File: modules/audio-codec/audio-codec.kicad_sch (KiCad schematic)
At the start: 1 part, among them U1 TLV320AIC3110IRHBR

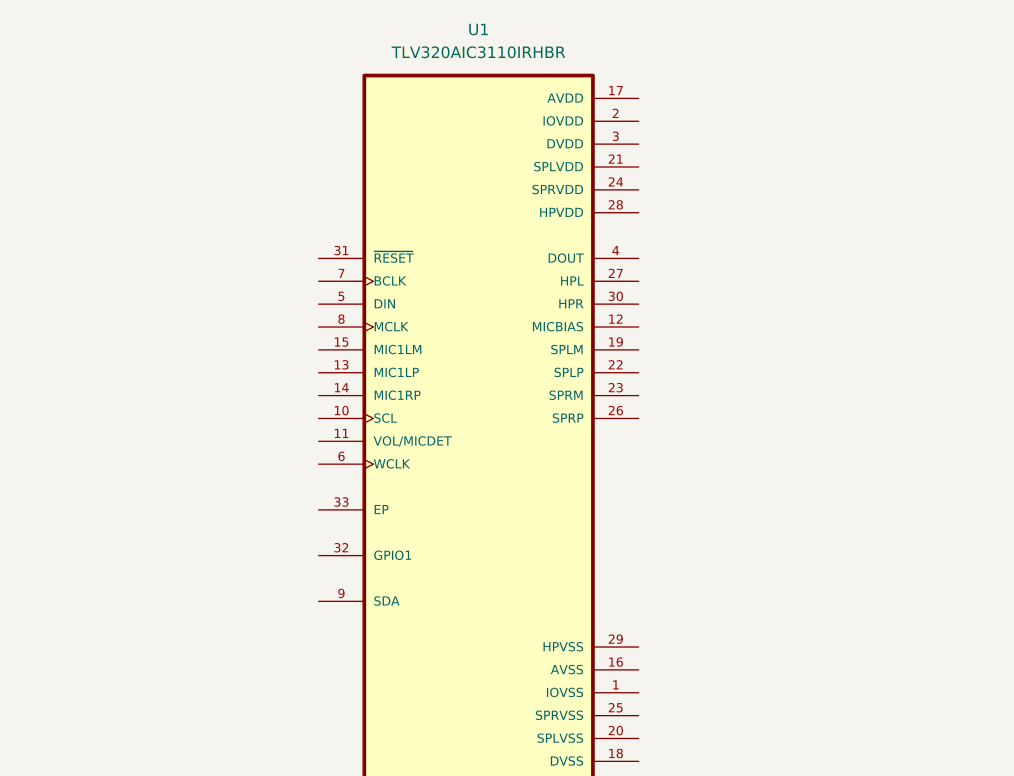
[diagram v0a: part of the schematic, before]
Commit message: add ADP5301 vreg and work on schematic
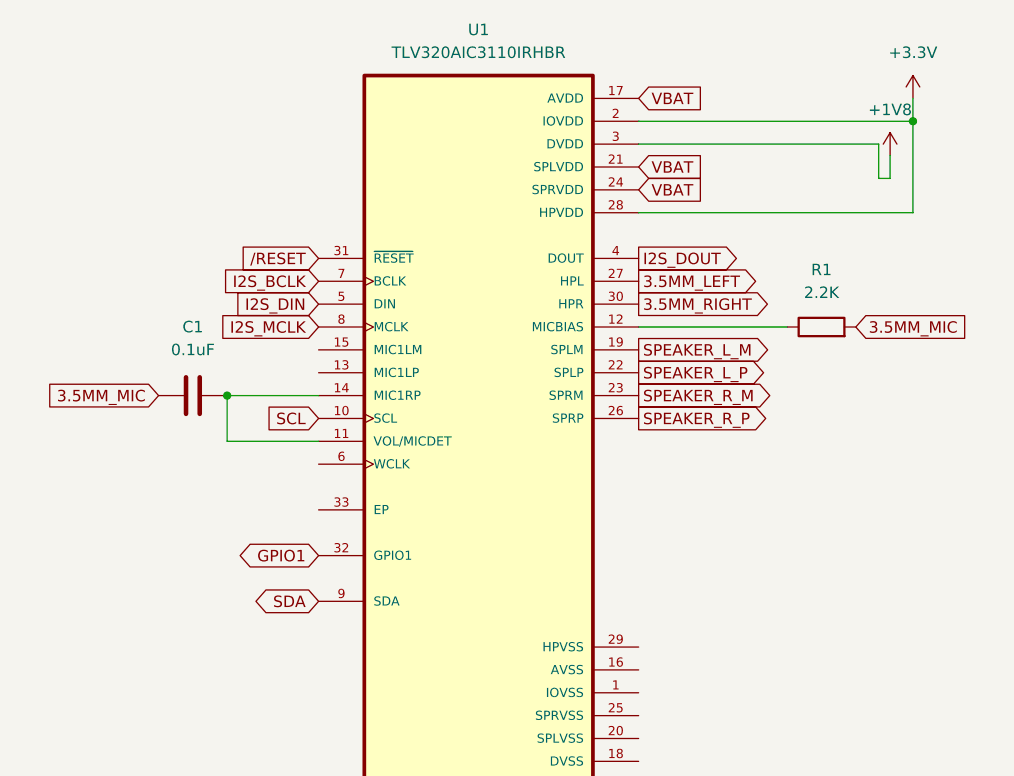
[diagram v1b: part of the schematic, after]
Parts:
- added C1: 0.1uF, symbol Device:C
- added R1: 2.2K, symbol Device:R
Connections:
- net SCL: now reaches U1.10 (SCL)
- net at U1.11 (VOL/MICDET): now also U1.14 (MIC1RP), C1.1
- net at U1.12 (MICBIAS): now also R1.1
- net VBAT: now reaches U1.17 (AVDD)
- net VBAT: now also U1.21 (SPLVDD), U1.24 (SPRVDD)
- net SPEAKER_L_M: now reaches U1.19 (SPLM)
- net +3.3V: now reaches U1.2 (IOVDD)
- net +3.3V: now also U1.28 (HPVDD)
- net SPEAKER_L_P: now reaches U1.22 (SPLP)
- net SPEAKER_R_M: now reaches U1.23 (SPRM)
- net SPEAKER_R_P: now reaches U1.26 (SPRP)
- net 3.5MM_LEFT: now reaches U1.27 (HPL)
- net +1V8: now reaches U1.3 (DVDD)
- net 3.5MM_RIGHT: now reaches U1.30 (HPR)
- net /RESET: now reaches U1.31 (~{RESET})
- net GPIO1: now reaches U1.32 (GPIO1)
- net I2S_DOUT: now reaches U1.4 (DOUT)
- net I2S_DIN: now reaches U1.5 (DIN)
- net I2S_BCLK: now reaches U1.7 (BCLK)
- net I2S_MCLK: now reaches U1.8 (MCLK)
- net SDA: now reaches U1.9 (SDA)
- new net 3.5MM_MIC: C1.2, R1.2

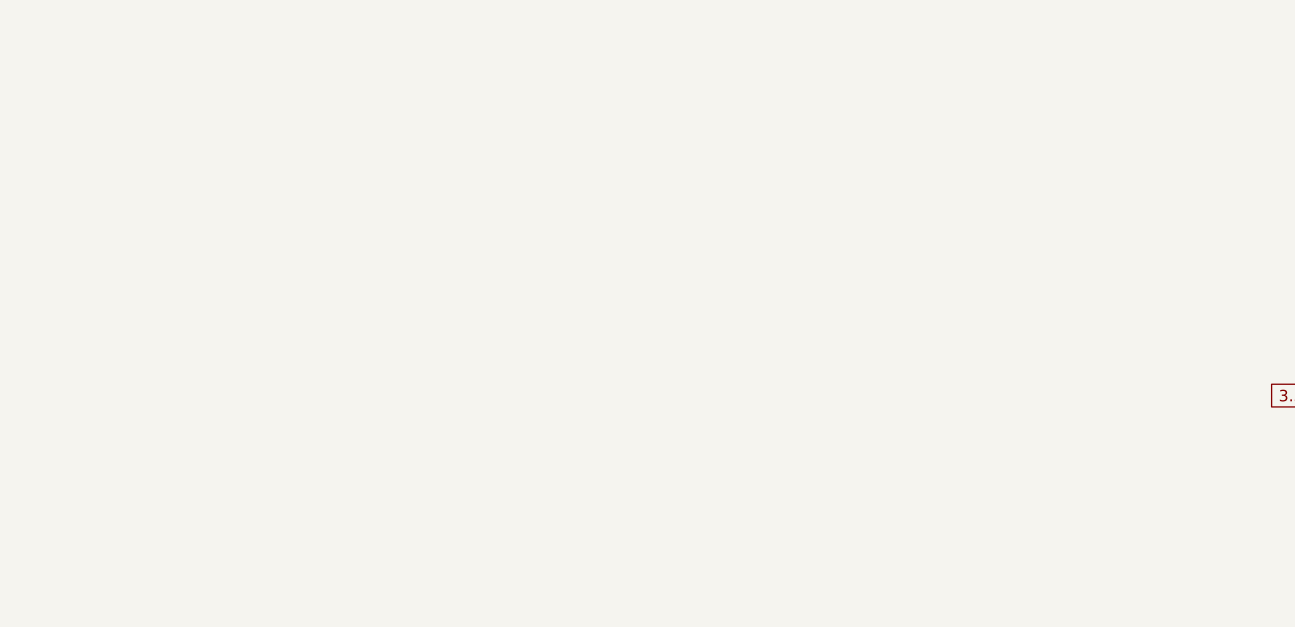
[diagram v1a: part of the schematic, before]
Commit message: more work on audio codec module
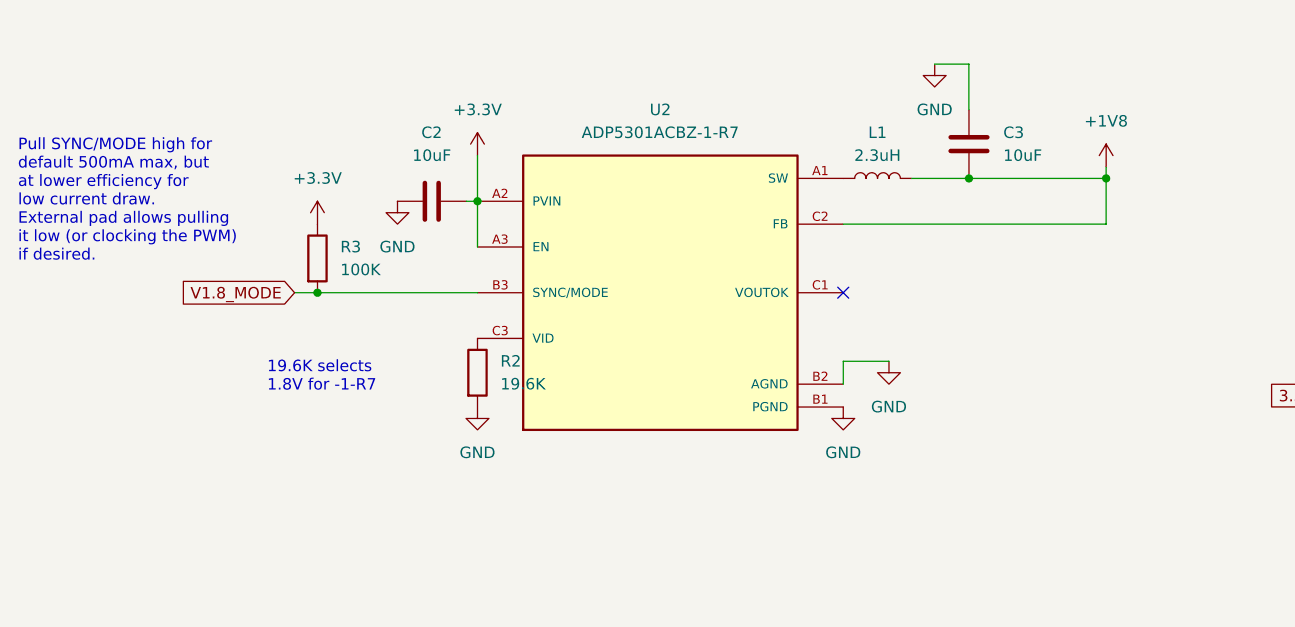
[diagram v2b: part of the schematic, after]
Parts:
- added C2, C3: 10uF, symbol Device:C
- added L1: 2.3uH, symbol Device:L
- added R2: 19.6K, symbol Device:R
- added R3: 100K, symbol Device:R
- added U2: ADP5301ACBZ-1-R7, ADP5301ACBZ-1-R7:BGA9C50P3X3_187X165X66N, symbol ADP5301ACBZ-1-R7:ADP5301ACBZ-1-R7
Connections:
- net +1V8: now also C3.1, L1.2, U2.C2 (FB)
- net +3.3V: now also C2.2, R3.1, U2.A2 (PVIN), U2.A3 (EN)
- new net: L1.1, U2.A1 (SW)
- new net: R2.1, U2.C3 (VID)
- new net GND: C2.1, C3.2, R2.2, U2.B1 (PGND), U2.B2 (AGND)
- new net V1.8_MODE: R3.2, U2.B3 (SYNC/MODE)
- no-connect marks 0 -> 1
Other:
- note added: "19.6K selects 1.8V for -1-R7"
- note added: "Pull SYNC/MODE high for default 500mA max, but at lower efficiency for low current draw. External pad allows pulling it low (or clocking the PWM) if desired."

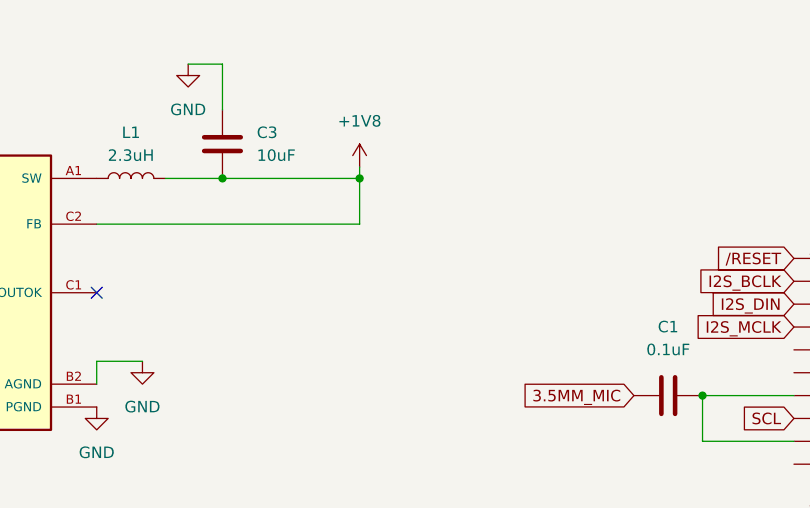
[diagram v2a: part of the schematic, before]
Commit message: add 1.8V test point
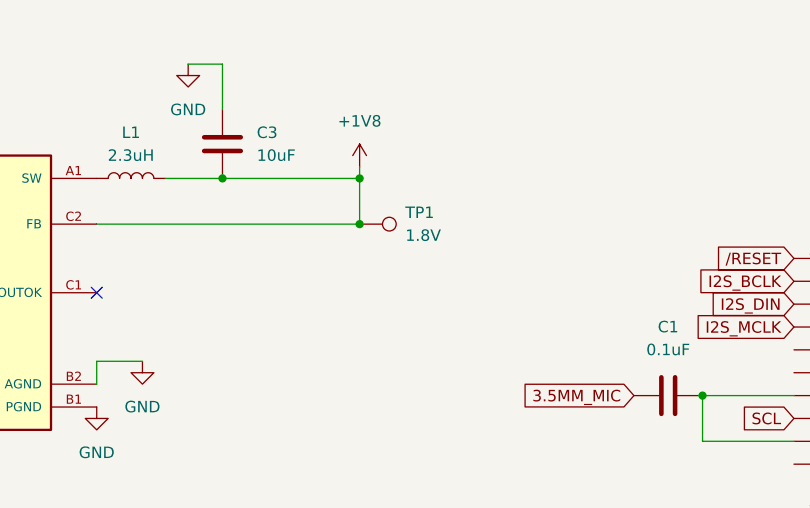
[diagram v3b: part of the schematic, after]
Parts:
- added TP1: 1.8V, symbol Connector:TestPoint
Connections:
- net +1V8: now also TP1.1
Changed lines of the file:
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@@
+	)
+	(junction
+		(at 134.62 57.15)
+		(diameter 0)
+		(color 0 0 0 0)
 	)
 	(junction
@@
 					(unit 1)
 				)
+			)
+		)
+	)
+	(symbol
+		(lib_id "Connector:TestPoint")
+		(at 134.62 57.15 270)
+		(unit 1)
+		(exclude_from_sim no)
+		(in_bom yes)
+		(on_board yes)
+		(dnp no)
+		(fields_autoplaced yes)
+		(property "Reference" "TP1"
+			(at 139.7 55.8799 90)
+			(effects
+				(font
+					(size 1.27 1.27)
+				)
+				(justify left)
+			)
+		)
+		(property "Value" "1.8V"
+			(at 139.7 58.4199 90)
+			(effects
+				(font
+					(size 1.27 1.27)
+				)
+				(justify left)
+			)
+		)
+		(property "Footprint" ""
+			(at 134.62 62.23 0)
+			(effects
+				(font
+					(size 1.27 1.27)
+				)
+				(hide yes)
+			)
+		)
+		(property "Datasheet" "~"
+			(at 134.62 62.23 0)
+			(effects
+				(font
+					(size 1.27 1.27)
+				)
+				(hide yes)
+			)
+		)
+		(property "Description" "test point"
+			(at 134.62 57.15 0)
+			(effects
+				(font
+					(size 1.27 1.27)
+				)
+				(hide yes)
+			)
+		)
+		(pin "1"
+		)
+		(instances
+			(project ""
+				(path "/e0031877-65b0-4e57-86fe-bc20869de862"
+					(reference "TP1")
+					(unit 1)
+				)

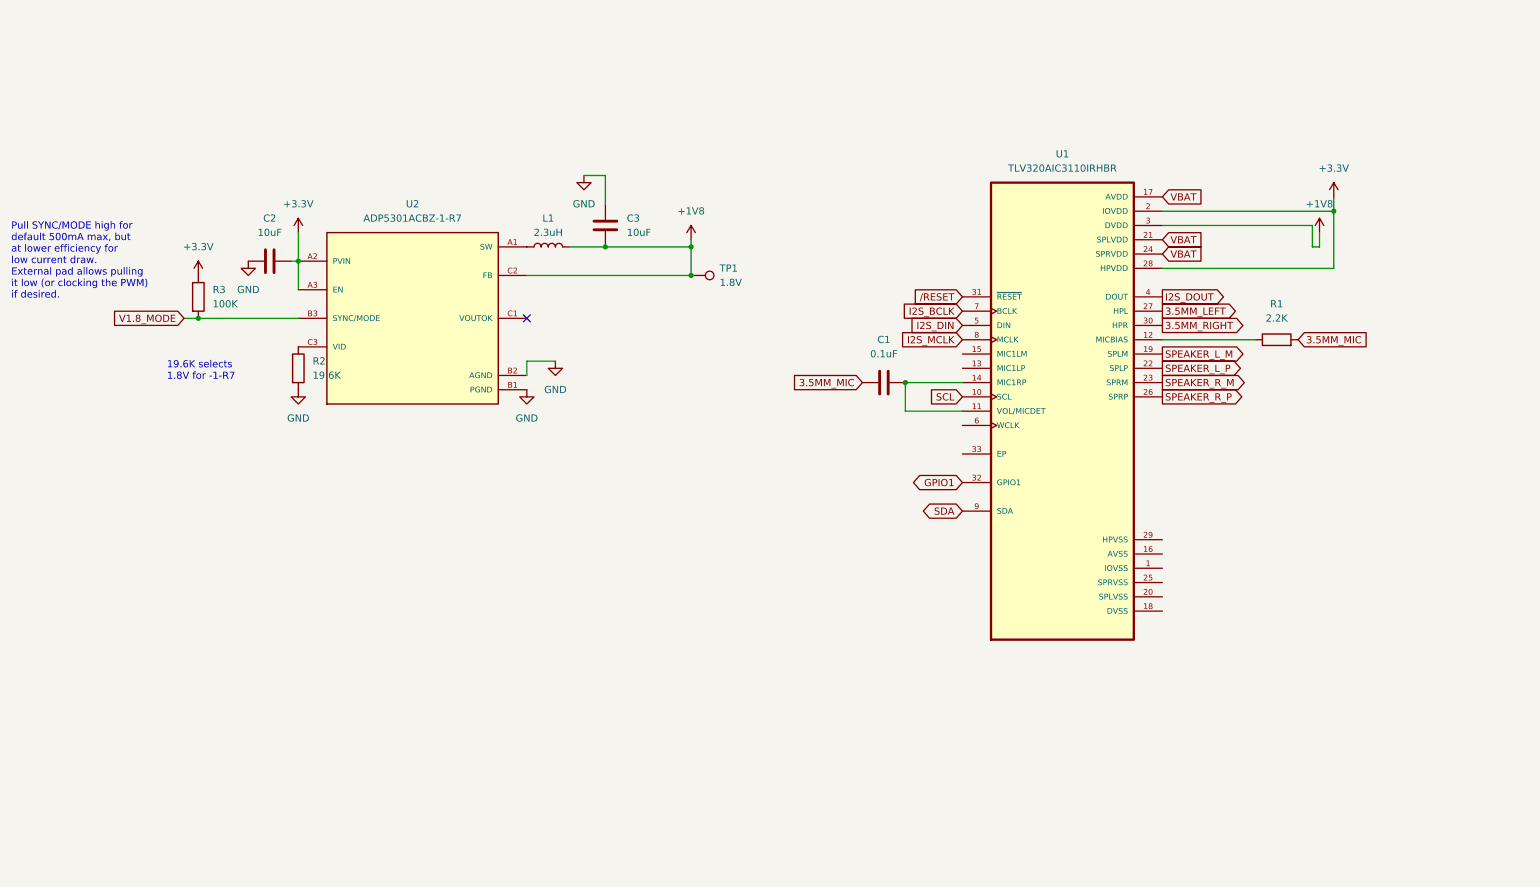
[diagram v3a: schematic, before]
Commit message: add remaining passives for audio codec module schematic
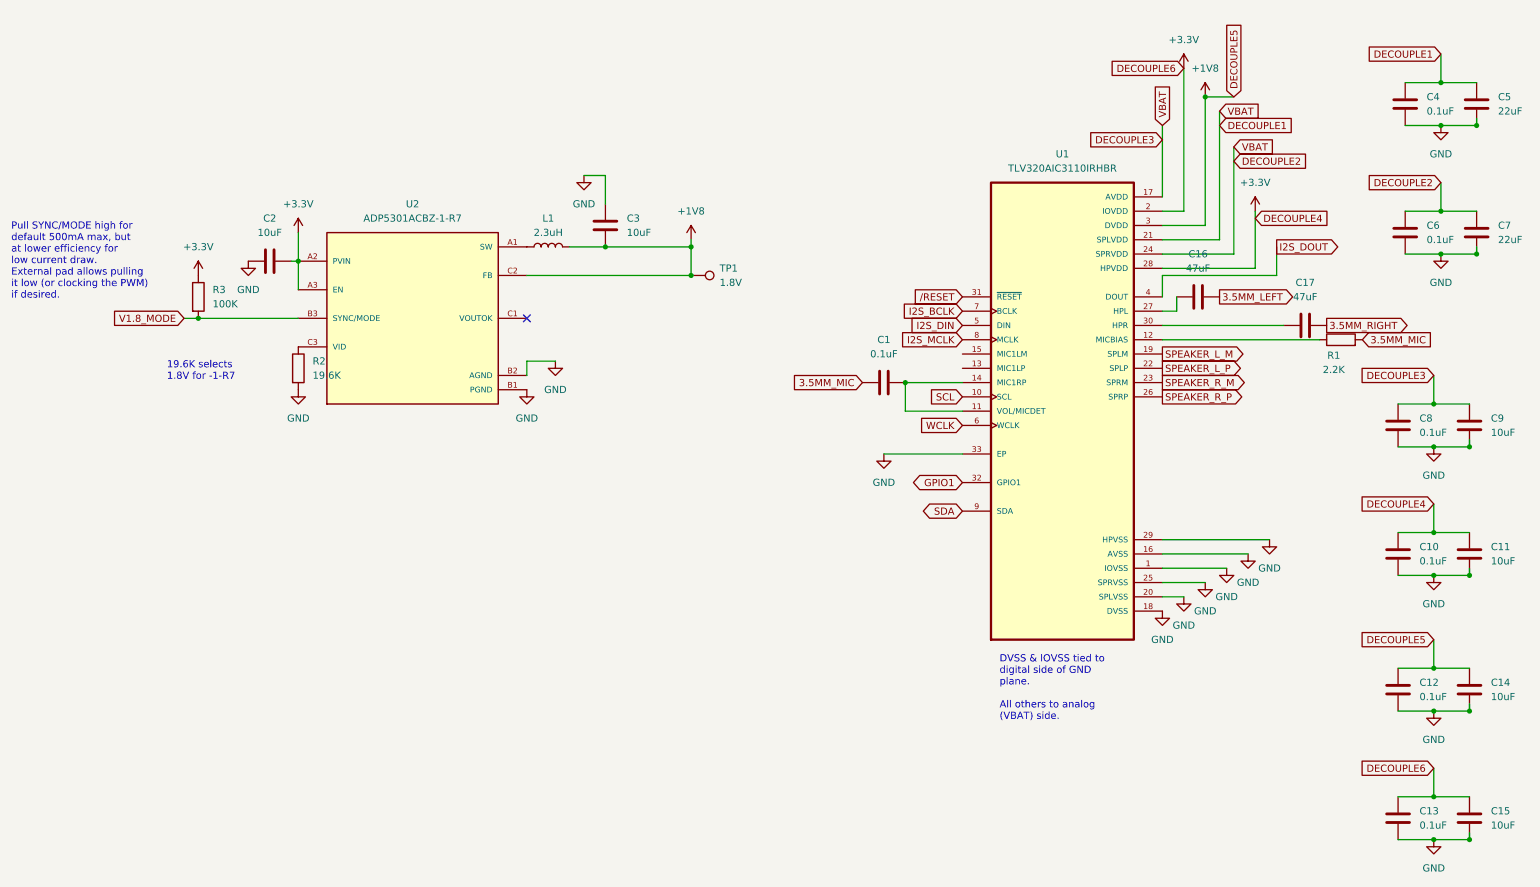
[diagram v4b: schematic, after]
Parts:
- added C10, C12, C13, C4, C6, C8: 0.1uF, symbol Device:C
- added C11, C14, C15, C9: 10uF, symbol Device:C
- added C16, C17: 47uF, symbol Device:C
- added C5, C7: 22uF, symbol Device:C
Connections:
- net +1V8: now also C12.1, C14.1
- net +3.3V: now also C10.1, C11.1, C13.1, C15.1
- net 3.5MM_LEFT: now also C16.2; no longer U1.27 (HPL)
- net 3.5MM_RIGHT: now also C17.2; no longer U1.30 (HPR)
- net GND: now also U1.1 (IOVSS), U1.16 (AVSS), U1.18 (DVSS), U1.20 (SPLVSS), U1.25 (SPRVSS), U1.29 (HPVSS), U1.33 (EP), C10.2, C11.2, C12.2, C13.2, C14.2, C15.2, C4.2, C5.2, C6.2, C7.2, C8.2, C9.2
- net WCLK: now reaches U1.6 (WCLK)
- net VBAT renamed DECOUPLE1
- net DECOUPLE1: now also C4.1, C5.1, C6.1, C7.1, C8.1, C9.1
- new net: C16.1, U1.27 (HPL)
- new net: C17.1, U1.30 (HPR)
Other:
- note added: "DVSS & IOVSS tied to digital side of GND plane. All others to analog (VBAT) side."
- moved on the sheet: R1

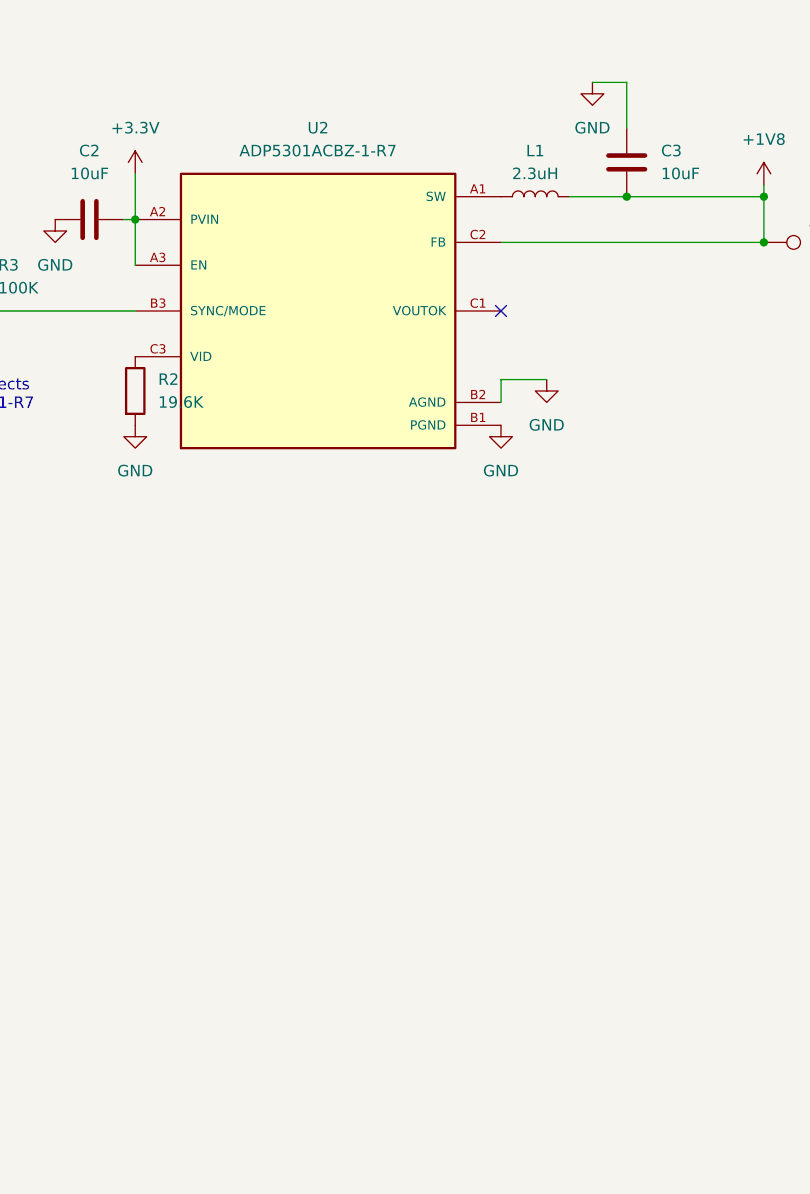
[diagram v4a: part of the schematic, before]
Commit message: update 2x11 module footprint. Work on PCB layout of audio codec module
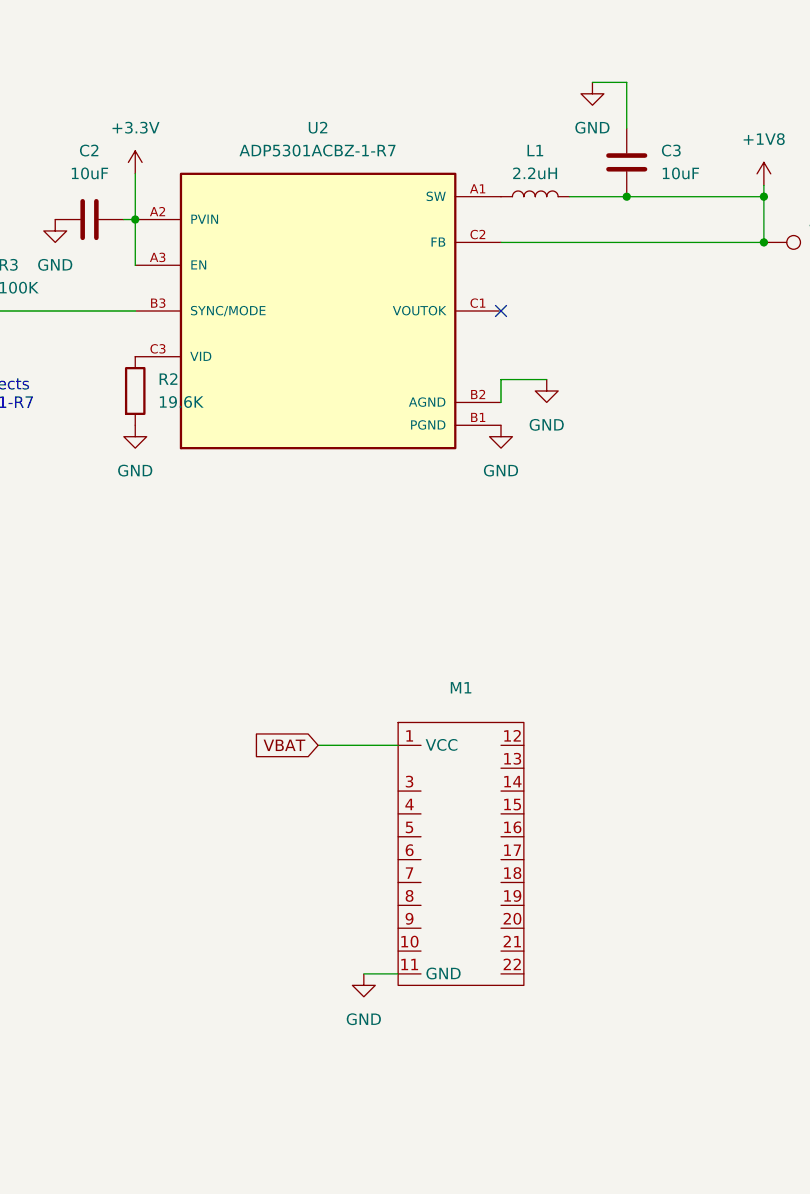
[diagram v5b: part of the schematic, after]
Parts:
- added M1: ~, MegaCastle:MegaCastle2x11Wide-Module-I13.2x22.25, symbol MegaCastle:MegaCastle2x11-Module
- C1, C10, C11, C12, C13, C14, C15, C16, C17, C2, C3, C4, C5, C6, C7, C8, C9: footprint (none) -> Capacitor_SMD:C_0603_1608Metric
- L1: value 2.3uH -> 2.2uH; footprint (none) -> Inductor_SMD:L_0805_2012Metric
- R1, R2, R3: footprint (none) -> Resistor_SMD:R_0603_1608Metric
- TP1: footprint (none) -> TestPoint:TestPoint_Pad_D1.0mm
- U2: footprint ADP5301ACBZ-1-R7:BGA9C50P3X3_187X165X66N -> BGA9C50P3X3_187X165X66N
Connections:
- net DECOUPLE1: now also M1.1 (VCC)
- net GND: now also M1.11 (GND)
